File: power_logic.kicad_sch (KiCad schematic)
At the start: 19 parts, among them J10 Barrel_Jack_MountingPin, U15 TPS62933, U2 AMS1117-3.3

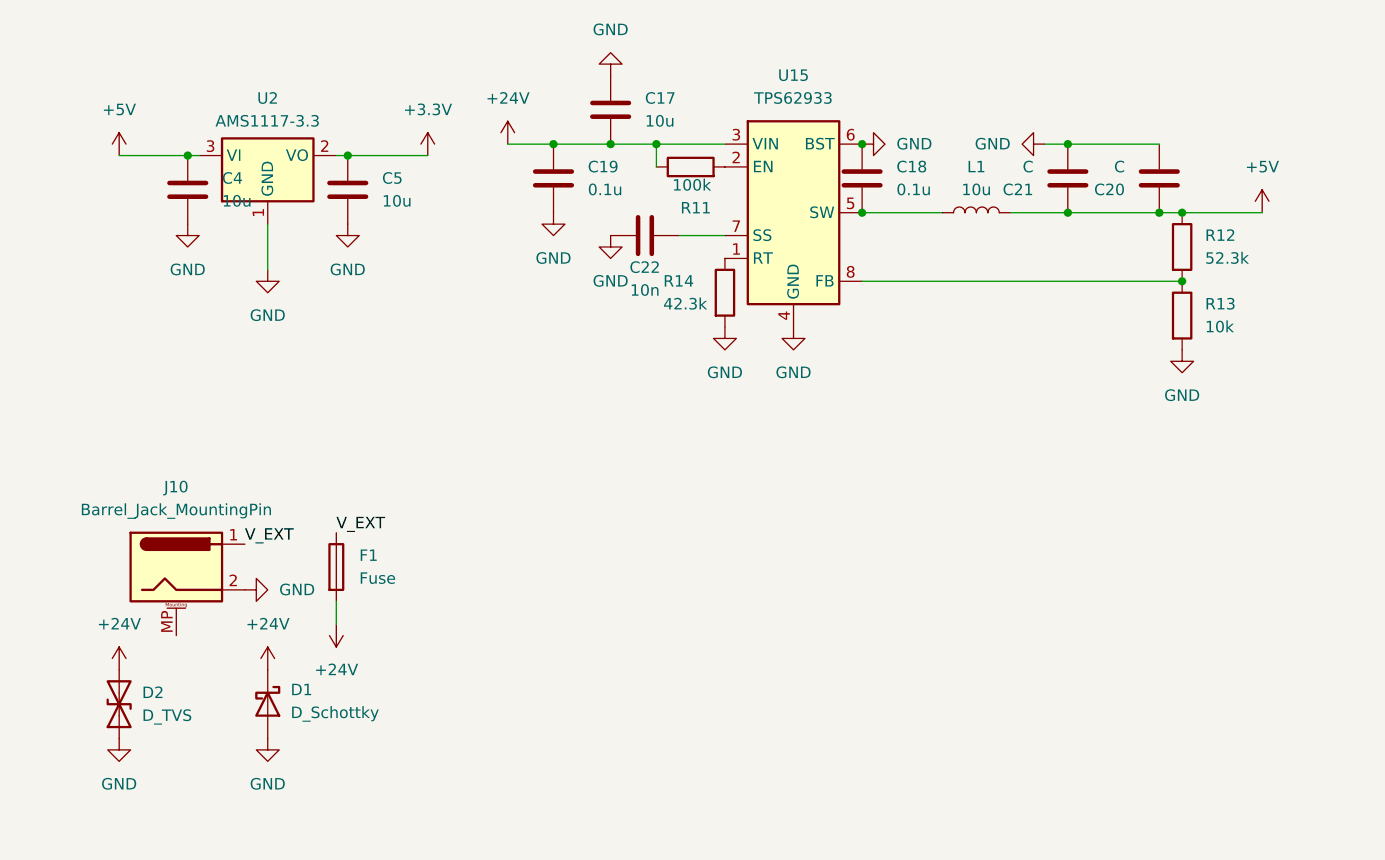
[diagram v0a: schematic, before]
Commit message: Fixed most ERC checks
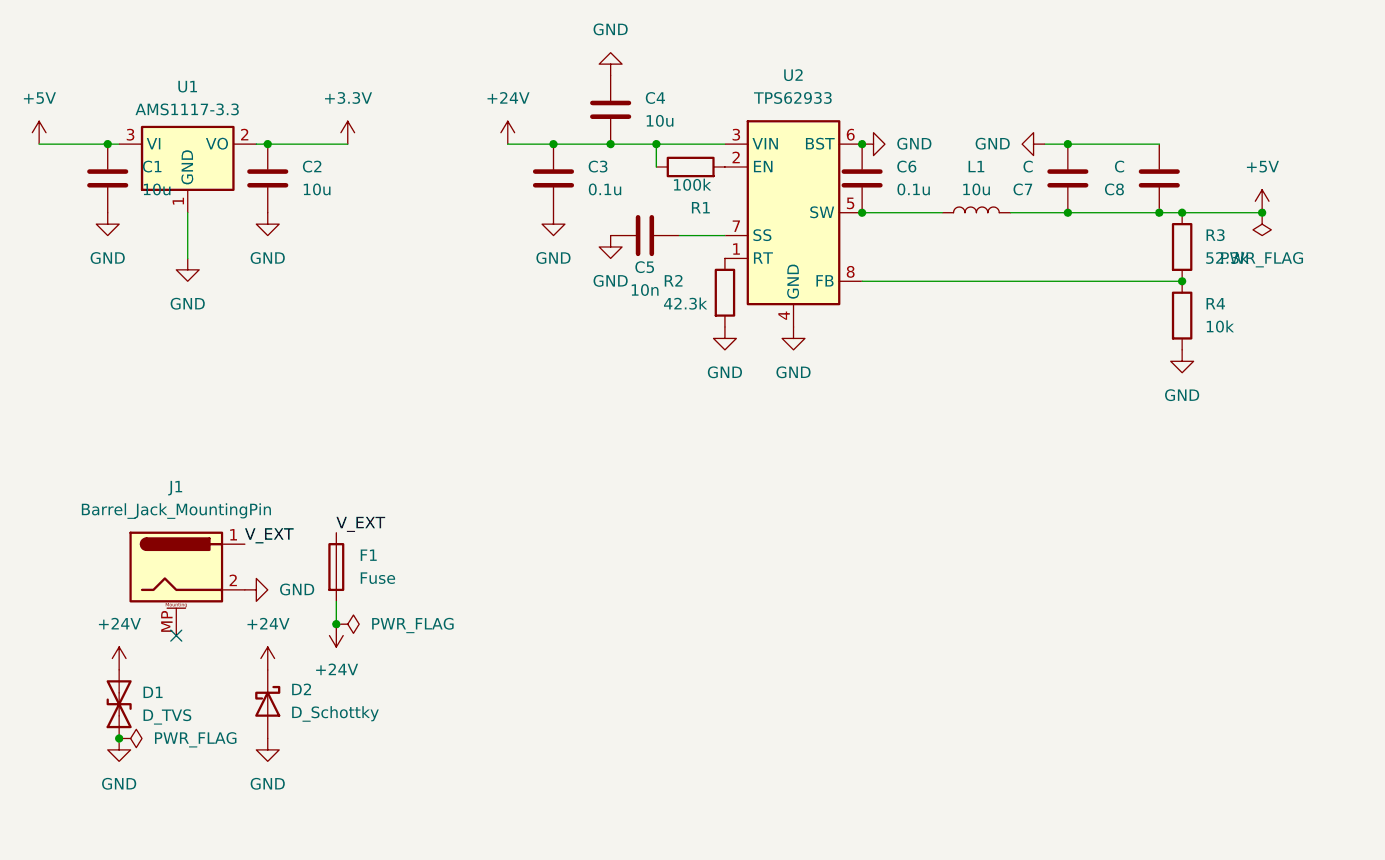
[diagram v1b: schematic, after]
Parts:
- renumbered C4 to C1, C5 to C2, C19 to C3, C17 to C4, C22 to C5, C18 to C6, C21 to C7, C20 to C8, D2 to D1, D1 to D2, J10 to J1, R11 to R1, R14 to R2, R12 to R3, R13 to R4, U2 to U1, U15 to U2
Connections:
- no-connect marks 0 -> 1
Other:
- moved on the sheet: C1, C2, U1

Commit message: Footprinting done (warnings on schematic side but pcb import works fine)
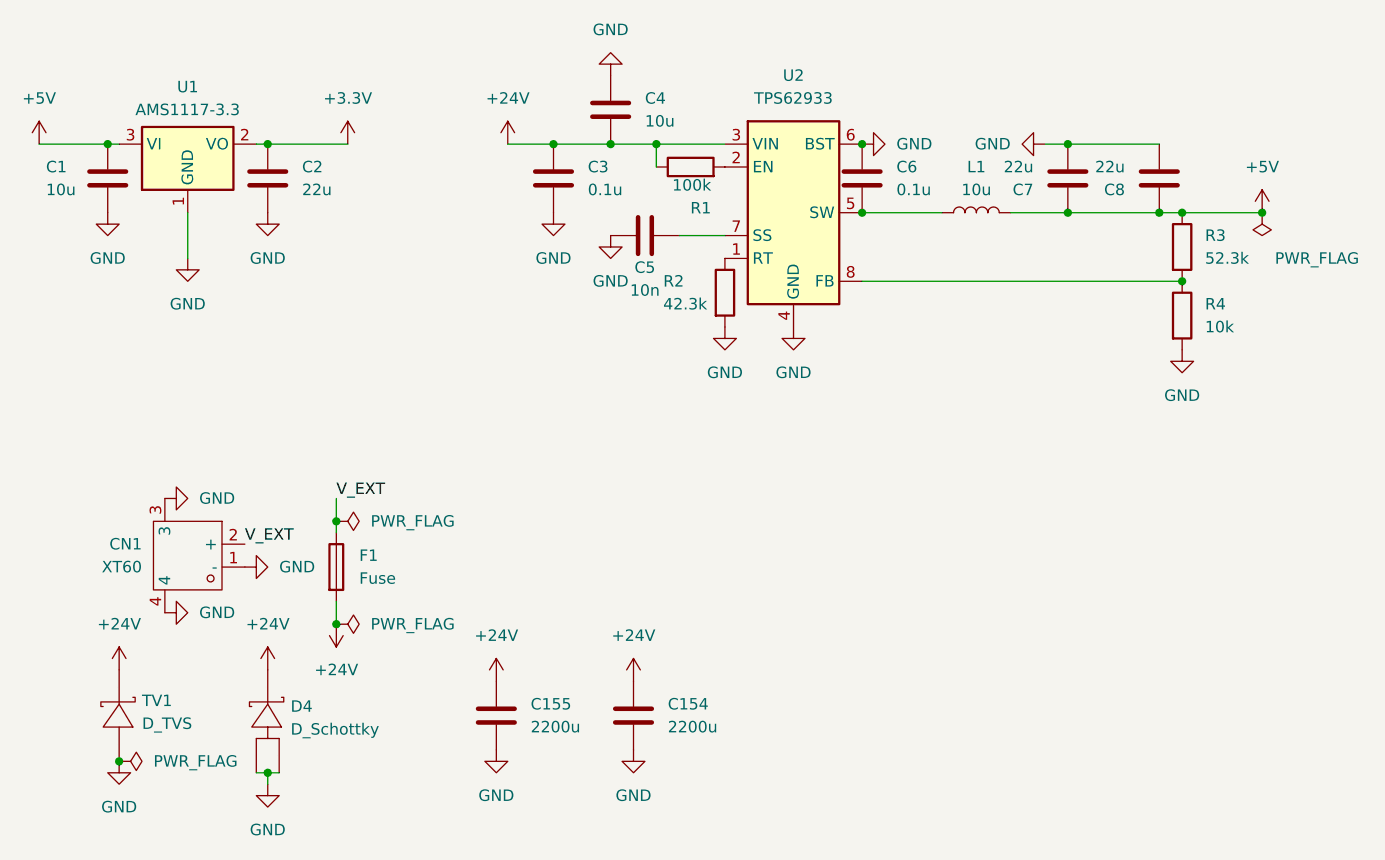
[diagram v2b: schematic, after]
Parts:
- removed D1: D_TVS, symbol Device:D_TVS
- removed D2: D_Schottky, symbol Device:D_Schottky
- removed J1: Barrel_Jack_MountingPin, symbol Connector:Barrel_Jack_MountingPin
- added C154, C155: 2200u, Capacitor_SMD:CAP-SMD_BD18.0-L19.0-W19.0-FD_EEEFK1E472SV, symbol Device:C
- added CN1: XT60, XT60-PW-M:CONN-TH_XT60PW-M, symbol XT60_Header:XT60PW-M
- added D4: D_Schottky, Diode_SMD:TO-277_3P-L5.4-W4.0-LS6.5-BR, symbol Diode:SL1545
- added TV1: D_TVS, Diode_SMD:Diode_SMC_L7.1-W6.2-LS8.1-R-RD, symbol Diode:SMCJ28A
- C1: footprint (none) -> Capacitor_Tantalum_SMD:CP_EIA-3216-18_Kemet-A; LCSC Part # (none) -> C7171; Voltage Rating (none) -> 16V
- C2: value 10u -> 22u; footprint (none) -> Capacitor_Tantalum_SMD:CP_EIA-3216-18_Kemet-A; LCSC Part # (none) -> C7183; Voltage Rating (none) -> 6.6V
- C3, C6: footprint (none) -> Capacitor_SMD:C_0603_1608Metric; LCSC Part # (none) -> C14633; Voltage Rating (none) -> 50V
- C4: footprint (none) -> Capacitor_SMD:C_1210_3225Metric; LCSC Part # (none) -> C116808; Voltage Rating (none) -> 50V
- C5: footprint (none) -> Capacitor_SMD:C_0603_1608Metric; LCSC Part # (none) -> C1589; Voltage Rating (none) -> 50V
- C7, C8: value C -> 22u; footprint (none) -> Capacitor_SMD:C_1206_3216Metric; LCSC Part # (none) -> C12891; Voltage Rating (none) -> 25V
- F1: footprint (none) -> Fuse:F1206_32V_12A; LCSC Part # (none) -> C126815
- L1: footprint (none) -> Inductor_SMD:IND-SMD_L10.4-W10.3; LCSC Part # (none) -> C9935; Saturation Current (none) -> 5.6A
- R1, R2, R3, R4: footprint (none) -> Resistor_SMD:R_0603_1608Metric
- U1: LCSC Part # (none) -> C6186
- U2: LCSC Part # (none) -> C5219272
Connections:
- net +24V: now also C154.1, C155.1, D4.2 (K), TV1.2 (K)
- net GND: now also C154.2, C155.2, CN1.1 (-), CN1.3, CN1.4, D4.1 (A), D4.3 (A), TV1.1 (A)
- net V_EXT: now also CN1.2 (+)
- no-connect marks 1 -> 0

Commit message: Minor schematic changes
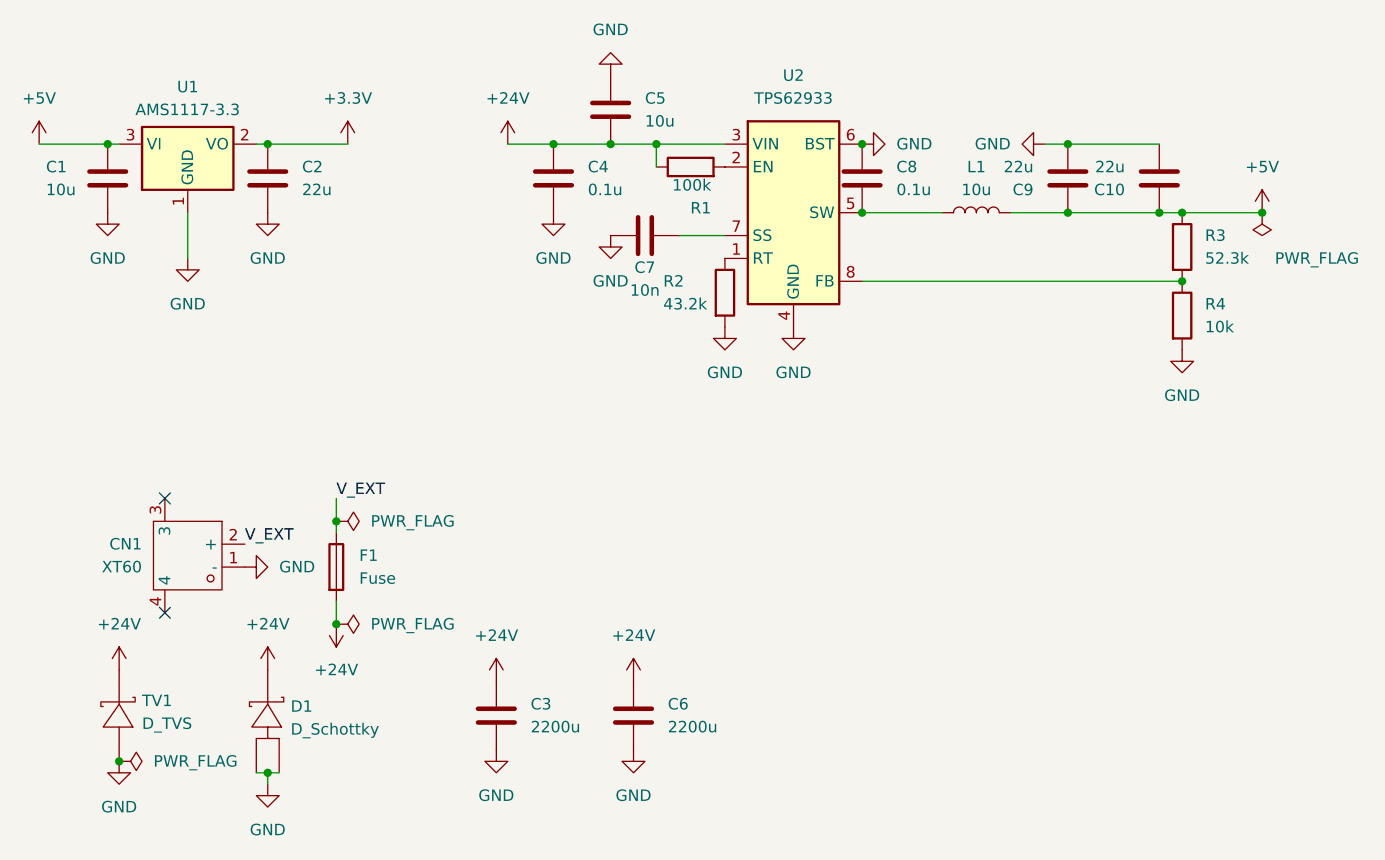
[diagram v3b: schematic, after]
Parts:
- R2: value 42.3k -> 43.2k; LCSC Part # (none) -> C22356315
- R3: LCSC Part # (none) -> C22369875
- renumbered C8 to C10, C155 to C3, C3 to C4, C4 to C5, C154 to C6, C5 to C7, C6 to C8, C7 to C9, D4 to D1
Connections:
- net GND: no longer CN1.3, CN1.4
- no-connect marks 0 -> 2
